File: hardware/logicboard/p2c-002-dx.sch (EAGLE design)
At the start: 50 parts, among them IC1 74LS07N, K1 G5V1, T1 2SC1815

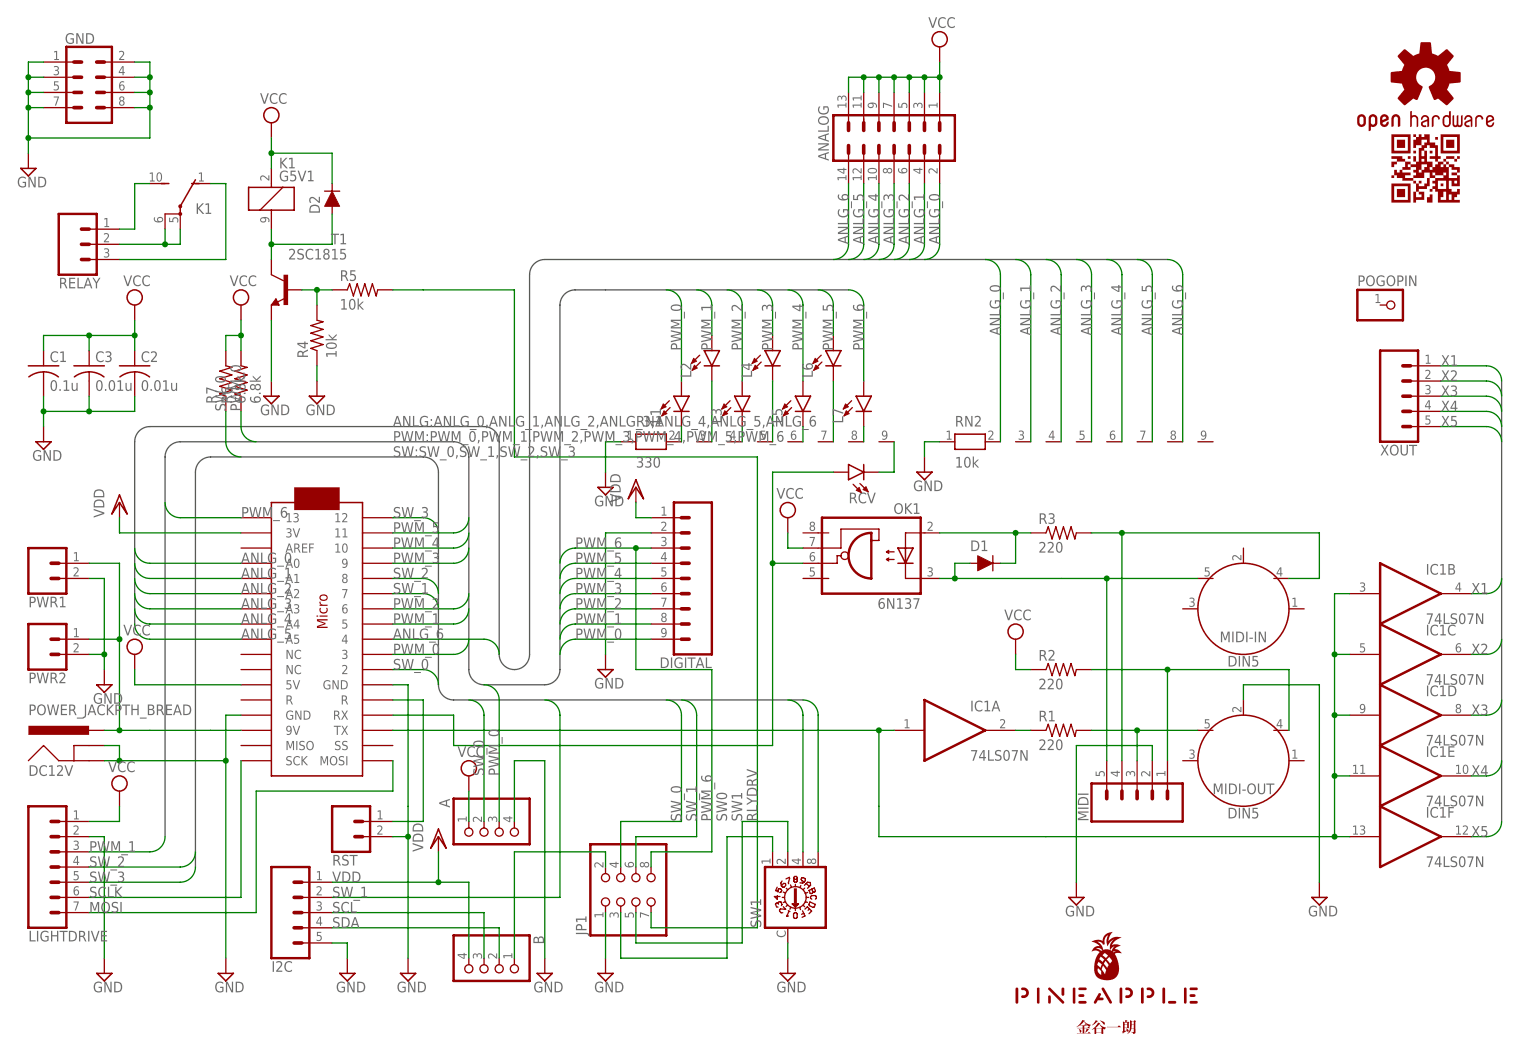
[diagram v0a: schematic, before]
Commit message: Removed unnecessary parts from DX board.
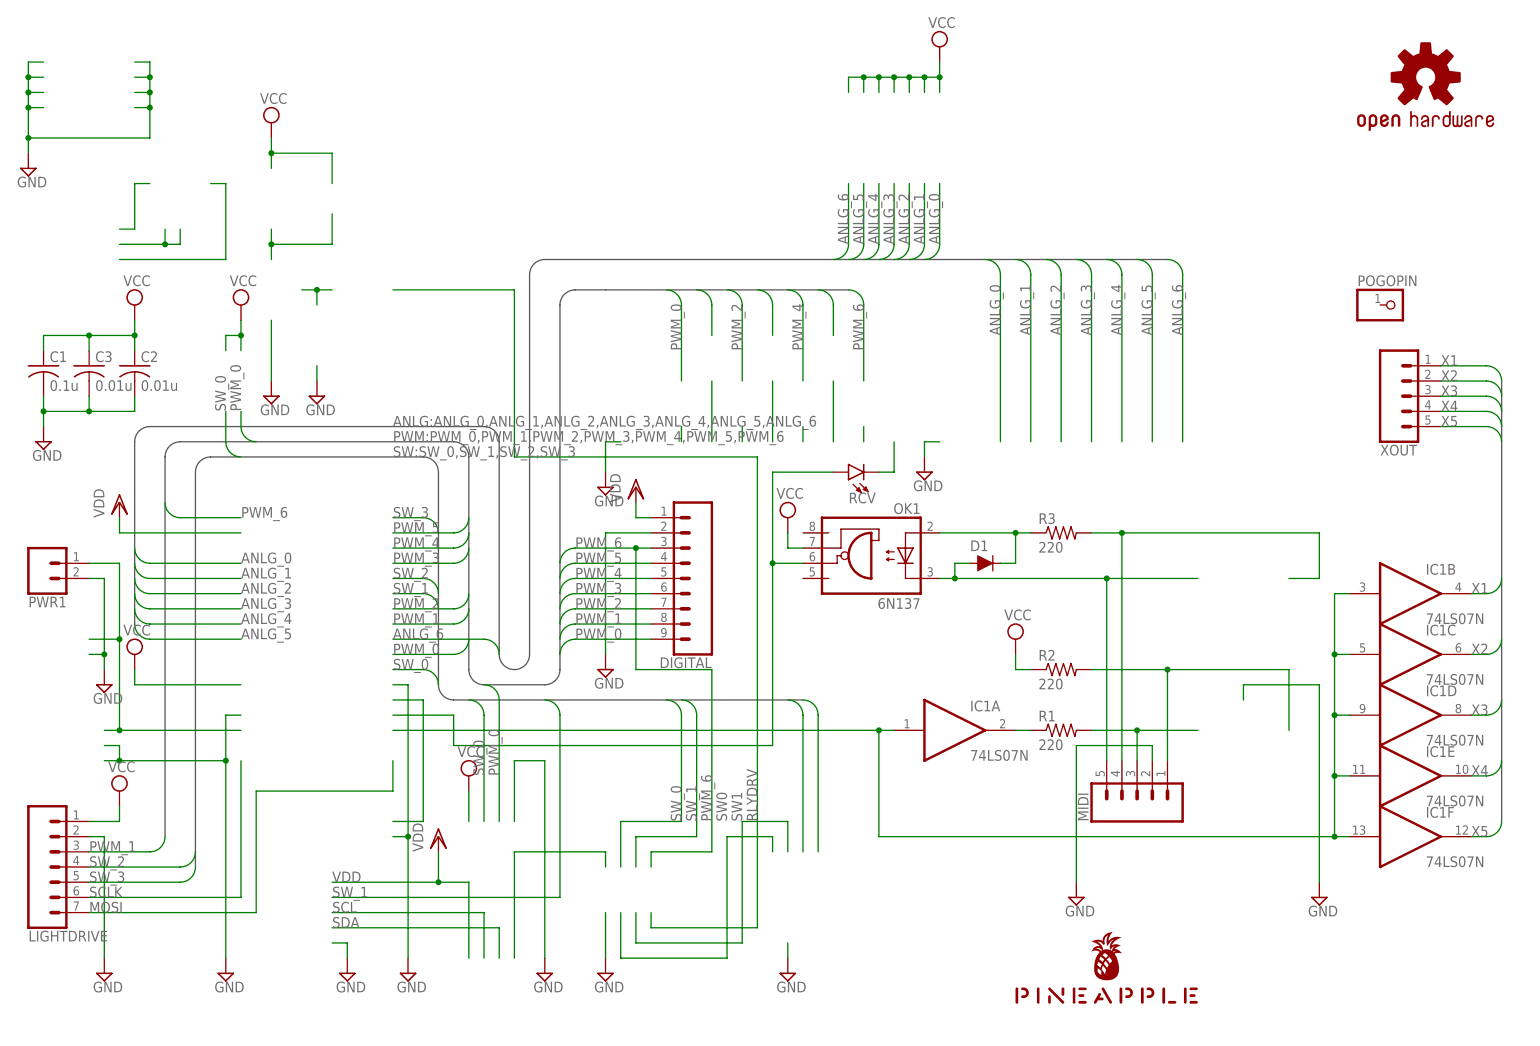
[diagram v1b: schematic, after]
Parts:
- removed A, B: (no value), pinhead:PINHD-1X4
- removed ANALOG: (no value), con-ml:ML14L
- removed D2: DIODE-1N4148, SparkFun-DiscreteSemi:DIODE-1N4148
- removed DC12V: POWER_JACKPTH_BREAD, SparkFun-Connectors:POWER_JACKPTH_BREAD
- removed GND: (no value), SparkFun-Connectors:CONN_04X2
- removed I2C: (no value), SparkFun-Connectors:CONN_05SMD2
- removed JP1: (no value), pinhead:PINHD-2X4
- removed K1: G5V1, relay:G5V1
- removed L1, L2, L3, L4, L5, L6, L7: (no value), SparkFun-LED:LED-3MM-NO_SILK
- removed MIDI-IN, MIDI-OUT: DIN5, SparkFun-Connectors:DIN5
- removed PWR2, RST: (no value), SparkFun-Connectors:CONN_02JST-PTH-2
- removed R4, R5: 10k, resistor:R-US_0204/5
- removed R6, R7: 6.8k, resistor:R-US_0204/5
- removed RELAY: (no value), SparkFun-Connectors:CONN_03JST-PTH
- removed RN1: 330, resistor-net:RN08
- removed RN2: 10k, resistor-net:RN08
- removed SW1: (no value), switch-dil:A1353HEX
- removed T1: 2SC1815, transistor:2SC1815
- removed U$2: ARDUINOMICRO, adafruit:ARDUINOMICRO
- removed U$3: KANAYA768_SILK, pineapple:KANAYA768_SILK
- removed U$4: CARDQRCODE450_SILK, pineapple:CARDQRCODE450_SILK
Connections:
- removed net ANLG_0: ANALOG.2, RN2.2, U$2.A0
- removed net ANLG_1: ANALOG.4, RN2.3, U$2.A1
- removed net ANLG_2: ANALOG.6, RN2.4, U$2.A2
- removed net ANLG_3: ANALOG.8, RN2.5, U$2.A3
- removed net ANLG_4: ANALOG.10, RN2.6, U$2.A4
- removed net ANLG_5: ANALOG.12, RN2.7, U$2.A5
- removed net ANLG_6: ANALOG.14, RN2.8, U$2.4
- removed net I2CENABLE: B.1, JP1.2
- removed net LED1K: L1.C, RN1.2
- removed net LED2K: L2.C, RN1.3
- removed net LED3K: L3.C, RN1.4
- removed net LED4K: L4.C, RN1.5
- removed net LED5K: L5.C, RN1.6
- removed net LED6K: L6.C, RN1.7
- removed net LED7K: L7.C, RN1.8
- removed net RELAYCOM: K12.P, K12.P@1, RELAY.2
- removed net RELAYDRIVE: R4.2, R5.1, T1.B
- removed net RELAYNC: K12.O, RELAY.3
- removed net RELAYNO: K12.S, RELAY.1
- removed net RELAYTR: D2.A, K11.2, T1.C
- removed net RLYDRV: JP1.7, R5.2
- removed net RST: RST.1, U$2.R@2
- removed net SCL: B.3, I2C.3
- removed net SDA: B.2, I2C.4
- removed net SW0: JP1.3, SW1.1
- removed net SW1: JP1.5, SW1.2
- removed net SW_0: A.2, JP1.4, R7.1, U$2.2
- removed net SW_1: I2C.2, JP1.6, U$2.7
- net GND: no longer A.4, DC12V.GND, DC12V.GNDBREAK, GND.1, GND.2, GND.3, GND.4, GND.5, GND.6, GND.7, GND.8, I2C.5, JP1.1, MIDI-OUT.2, PWR2.2, R4.1, RN1.1, RN2.1, RST.2, SW1.C, T1.E, U$2.GND, U$2.GND@1
- net MIDIIN: no longer U$2.RX
- net MIDIIN+: no longer MIDI-IN.4
- net MIDIIN-: no longer MIDI-IN.5
- net MIDIOUT: no longer U$2.TX
- net MIDIOUT+: no longer MIDI-OUT.4
- net MIDIOUT-: no longer MIDI-OUT.5
- net MOSI: no longer U$2.MOSI
- net N$1: no longer RN1.9
- net PWM_0: no longer A.3, L1.A, R6.1, U$2.3
- net PWM_1: no longer L2.A, U$2.5
- net PWM_2: no longer L3.A, U$2.6
- net PWM_3: no longer L4.A, U$2.9
- net PWM_4: no longer L5.A, U$2.10
- net PWM_5: no longer L6.A, U$2.11
- net PWM_6: no longer JP1.8, L7.A, U$2.13
- net SCLK: no longer U$2.SCK
- net SW_2: no longer SW1.4, U$2.8
- net SW_3: no longer SW1.8, U$2.12
- net VCC: no longer A.1, ANALOG.1, ANALOG.11, ANALOG.13, ANALOG.3, ANALOG.5, ANALOG.7, ANALOG.9, D2.C, K11.1, R6.2, R7.2, U$2.5V
- net VDD: no longer B.4, I2C.1, U$2.3V
- net VIN: no longer DC12V.PWR, PWR2.1, U$2.9V

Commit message: Fixed QR code.
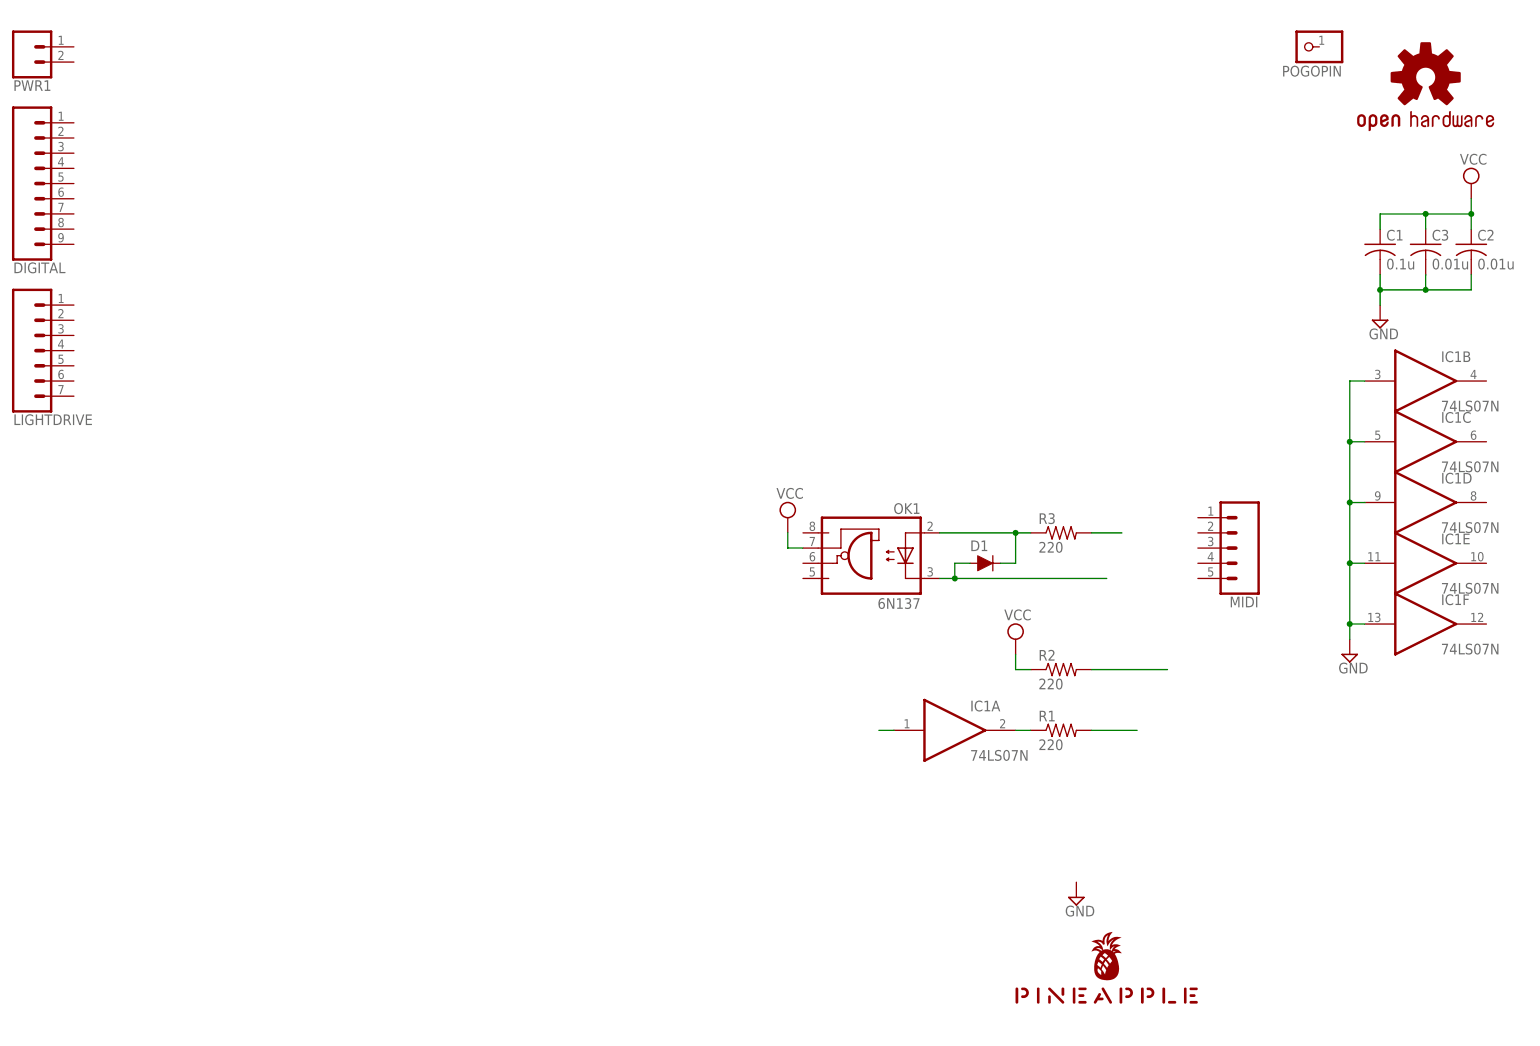
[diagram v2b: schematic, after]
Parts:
- removed RCV: (no value), SparkFun-LED:LED-3MM-NO_SILK
- removed XOUT: (no value), SparkFun-Connectors:CONN_05
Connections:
- removed net MIDIIN: OK1.VO, RCV.A
- removed net MIDIOUT: IC1A.I, IC1B.I, IC1C.I, IC1D.I, IC1E.I, IC1F.I
- removed net MOSI: LIGHTDRIVE.7
- removed net PWM_0: DIGITAL.9
- removed net PWM_1: DIGITAL.8, LIGHTDRIVE.3
- removed net PWM_2: DIGITAL.7
- removed net PWM_3: DIGITAL.6
- removed net PWM_4: DIGITAL.5
- removed net PWM_5: DIGITAL.4
- removed net PWM_6: DIGITAL.3
- removed net SCLK: LIGHTDRIVE.6
- removed net SW_2: LIGHTDRIVE.4
- removed net SW_3: LIGHTDRIVE.5
- removed net VDD: DIGITAL.1
- removed net VIN: PWR1.1
- removed net X1: IC1B.O, XOUT.1
- removed net X2: IC1C.O, XOUT.2
- removed net X3: IC1D.O, XOUT.3
- removed net X4: IC1E.O, XOUT.4
- removed net X5: IC1F.O, XOUT.5
- net GND: now also IC1B.I, IC1C.I, IC1D.I, IC1E.I, IC1F.I; no longer DIGITAL.2, LIGHTDRIVE.2, MIDI.2, PWR1.2
- net MIDIIN+: no longer MIDI.4
- net MIDIIN-: no longer MIDI.5
- net MIDIOUT+: no longer MIDI.1
- net MIDIOUT-: no longer MIDI.3
- net N$1: now also IC1A.I; no longer RCV.C
- net VCC: no longer LIGHTDRIVE.1
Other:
- moved on the sheet: C1, C2, C3, DIGITAL, IC1B, IC1C, IC1D, IC1E, IC1F, LIGHTDRIVE, MIDI, POGOPIN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
